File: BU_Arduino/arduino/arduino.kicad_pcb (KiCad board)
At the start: 2 copper layers, 52 parts, among them CON1 ICSP, J1 USB_A, J2 Barrel_Jack, J3 Power, J4 Digital, J5 Digital, J6 Analog, Q1 FDN340P, SW1 SW_Push_Dual, U1 NCP1117-12_TO252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

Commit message: Updated PCB Design Files
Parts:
- CON1, J3, J4, J5, J6: moved to F.Cu
- moved U1 145.3 mm to (102.5, 114.2), turned to 180 degrees
- moved J2 131.0 mm to (107.5, 124.3), turned to 0 degrees
- moved J3 125.3 mm to (144.4, 130.0), turned to 90 degrees
- moved U2 96.1 mm to (153.4, 104.9), turned to 180 degrees
- moved J1 87.6 mm to (182.1, 118.9), turned to 90 degrees
- moved J6 85.0 mm to (180.0, 130.0), turned to 270 degrees
- moved J4 82.1 mm to (135.3, 82.0), turned to 90 degrees
- moved CON1 69.2 mm to (182.6, 102.4), turned to 0 degrees
- moved J5 64.1 mm to (162.2, 82.0), turned to 90 degrees
- moved C15 63.0 mm to (124.6, 123.3)
- moved Q1 61.6 mm to (118.8, 111.6), turned to 180 degrees
- moved U4 58.8 mm to (102.1, 106.3)
- moved C3 49.7 mm to (109.9, 104.9)
- moved C22 47.5 mm to (102.8, 98.7), turned to 180 degrees
- moved C9 46.3 mm to (115.7, 123.3)
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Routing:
- net GND: track 18.2 -> 373.9 mm, vias 0 -> 9
- net +5V: track 19.0 -> 230.7 mm, vias 0 -> 12
- net /D7: track 0.00 -> 98.7 mm, vias 0 -> 3
- net +3V3: track 0.00 -> 97.9 mm, vias 0 -> 1
- net /VUSB: track 0.00 -> 74.4 mm, vias 0 -> 2
- net /D3/SCL: track 0.00 -> 72.5 mm, vias 0 -> 1
- net /VIN: track 16.1 -> 87.7 mm, vias 0 -> 1
- net /IO13: track 0.00 -> 71.0 mm, vias 0 -> 2
- net /D2/SDA: track 0.00 -> 69.0 mm, vias 0 -> 1
- net Net-(C16-Pad1): track 0.00 -> 59.0 mm, vias 0 -> 2
- net /D5: track 0.00 -> 59.0 mm, vias 0 -> 1
- net Net-(CON1-Pad5): track 0.00 -> 51.4 mm
- net /D0/RX: track 0.00 -> 47.8 mm, vias 0 -> 1
- net /AREF: track 0.00 -> 45.6 mm, vias 0 -> 4
- net /D6: track 0.00 -> 45.5 mm
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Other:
- board outline added: 89.7 x 55.1 mm
- board text added: "BUduino"

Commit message: Updated few files
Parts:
- C16, C18, C4, C5, C6, C8: footprint Capacitors_SMD:C_0805_HandSoldering -> Capacitors_SMD:C_0603_HandSoldering
- moved C8 100.8 mm to (204.0, 100.6)
- moved C21 82.7 mm to (183.7, 120.1)
- moved C22 76.9 mm to (179.3, 106.4)
- moved C3 62.8 mm to (170.7, 120.4), turned to 270 degrees
- moved C5 60.4 mm to (166.1, 118.4), turned to 270 degrees
- moved U4 56.4 mm to (158.5, 105.7)
- moved R11 50.9 mm to (161.3, 116.8), turned to 0 degrees
- moved SW1 46.2 mm to (209.8, 95.2), turned to 180 degrees
- moved U1 44.1 mm to (146.6, 115.3)
- moved D6 42.4 mm to (163.6, 104.6), turned to 270 degrees
- moved U3 41.4 mm to (156.5, 111.8), turned to 90 degrees
- moved D2 40.6 mm to (155.7, 121.4)
- moved R12 40.1 mm to (161.8, 108.7)
- moved R6 39.5 mm to (179.8, 117.9), turned to 90 degrees
- moved J2 38.1 mm to (145.5, 126.5)
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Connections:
- C6 pad 1: Net-(C6-Pad1) -> /AREF
- CON1 pad 5: Net-(CON1-Pad5) -> /RST
- D1 pad 2: Net-(CON1-Pad5) -> /RST
- J3 pad 3: /RESET -> /RST
- R3 pad 2: Net-(CON1-Pad5) -> /RST
- SW1 pad 1: Net-(CON1-Pad5) -> /RST
- U2 pad 13: Net-(CON1-Pad5) -> /RST
- U2 pad 42: Net-(C6-Pad1) -> /AREF
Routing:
- net /RST: track 0.00 -> 104.0 mm, vias 0 -> 4
- net Net-(CON1-Pad5): track 51.4 -> 0.00 mm
- net Net-(C16-Pad1): track 59.0 -> 10.6 mm, vias 2 -> 0
- net +3V3: track 97.9 -> 64.1 mm
- net /AREF: track 45.6 -> 73.4 mm, vias 4 -> 3
- net /D7: track 98.7 -> 73.6 mm, vias 3 -> 1
- net GND: track 373.9 -> 349.8 mm, vias 9 -> 11
- net /D2/SDA: track 69.0 -> 91.9 mm
- net /IO11: track 27.3 -> 46.2 mm
- net Net-(J1-Pad1): track 24.0 -> 5.67 mm, vias 2 -> 0
- net /VIN: track 87.7 -> 70.2 mm, vias 1 -> 2
- net /D0/RX: track 47.8 -> 31.1 mm
- net /IO13: track 71.0 -> 54.3 mm
- net Net-(C7-Pad2): track 27.9 -> 14.8 mm, vias 2 -> 0
- net Net-(J1-Pad2): track 18.5 -> 6.22 mm
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- added copper zone on B.Cu, net GND
- added copper zone on F.Cu, net GND
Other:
- board size 89.7 x 55.1 mm -> 78.2 x 55.6 mm

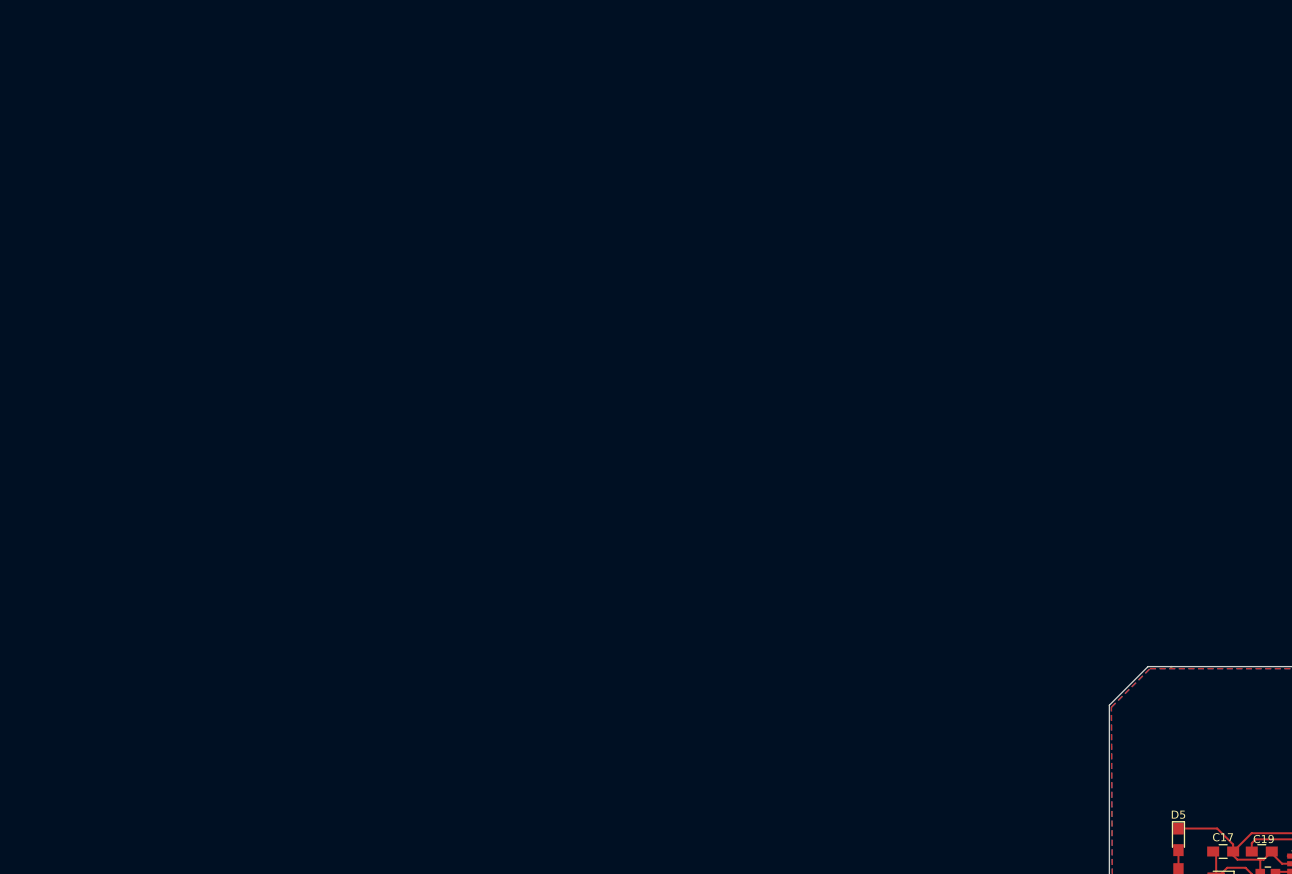
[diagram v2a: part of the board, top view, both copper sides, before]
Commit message: Added gnd planes stiching Vias
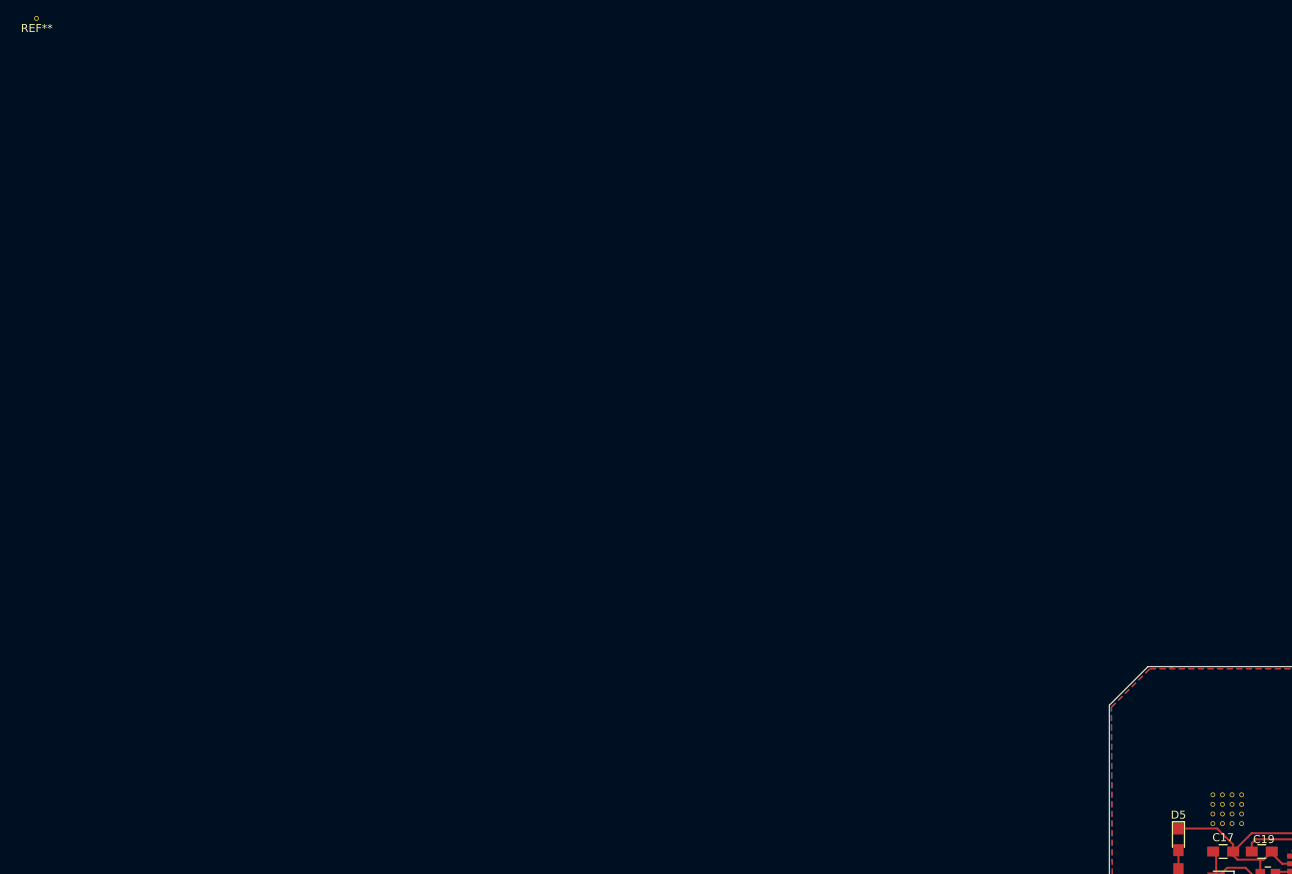
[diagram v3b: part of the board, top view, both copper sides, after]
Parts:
- added REF**: Via, arduino:Via, F.Cu at (150.7, 100.6)
- added REF**: Via, arduino:Via, F.Cu at (149.5, 98.2)
- added REF**: Via, arduino:Via, F.Cu at (148.3, 98.2)
- added REF**: Via, arduino:Via, F.Cu at (147.1, 98.2)
- added REF**: Via, arduino:Via, F.Cu at (150.7, 97.0)
- added REF**: Via, arduino:Via, F.Cu at (149.5, 97.0)
- added REF**: Via, arduino:Via, F.Cu at (148.3, 97.0)
- added REF**: Via-0.6mm, Via-0.6mm, F.Cu at (0.00, 0.00)
- added REF**: Via, arduino:Via, F.Cu at (147.1, 97.0)
- added REF**: Via, arduino:Via, F.Cu at (149.5, 100.6)
- added REF**: Via, arduino:Via, F.Cu at (148.3, 100.6)
- added REF**: Via, arduino:Via, F.Cu at (147.1, 100.6)
- added REF**: Via, arduino:Via, F.Cu at (150.7, 99.4)
- added REF**: Via, arduino:Via, F.Cu at (149.5, 99.4)
- added REF**: Via, arduino:Via, F.Cu at (148.3, 99.4)
- added REF**: Via, arduino:Via, F.Cu at (147.1, 99.4)
- added REF**: Via, arduino:Via, F.Cu at (150.7, 98.2)
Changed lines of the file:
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@@
 (kicad_pcb (version 4) (host pcbnew 4.0.7)
   (general
-    (links 145)
+    (links 161)
     (no_connects 0)
-    (area 131.316999 80.975999 212.511001 136.965)
+    (area -4.571904 -2.105 212.511001 136.965)
     (thickness 1.6)
     (drawings 16)
     (tracks 755)
     (zones 0)
-    (modules 52)
+    (modules 69)
     (nets 52)
   )
@@
     (mod_text_size 1 1)
     (mod_text_width 0.15)
-    (pad_size 1.2 0.75)
-    (pad_drill 0)
+    (pad_size 0.6 0.6)
+    (pad_drill 0.4)
     (pad_to_mask_clearance 0)
     (aux_axis_origin 0 0)
@@
       (psa4output false)
       (plotreference true)
-      (plotvalue true)
+      (plotvalue false)
       (plotinvisibletext false)
       (padsonsilk false)
@@
     (add_net "Net-(U4-Pad4)")
   )
+  (module arduino:Via (layer F.Cu)
+    (at 150.666 100.628)
+    (fp_text reference REF** (at 0.05 1.58) (layer F.SilkS) hide
+      (effects (font (size 1 1) (thickness 0.15)))
+    )
+    (fp_text value Via (at 0.01 -1.78) (layer F.Fab) hide
+      (effects (font (size 1 1) (thickness 0.15)))
+    )
+    (pad 1 thru_hole circle (at -0.02 0.02) (size 0.6 0.6) (drill 0.4) (layers *.Cu)
+      (net 2 GND) (zone_connect 2))
+  )
+  (module arduino:Via (layer F.Cu)
+    (at 149.466 100.628)
+    (fp_text reference REF** (at 0.05 1.58) (layer F.SilkS) hide
+      (effects (font (size 1 1) (thickness 0.15)))
+    )
+    (fp_text value Via (at 0.01 -1.78) (layer F.Fab) hide
+      (effects (font (size 1 1) (thickness 0.15)))
+    )
+    (pad 1 thru_hole circle (at -0.02 0.02) (size 0.6 0.6) (drill 0.4) (layers *.Cu)
+      (net 2 GND) (zone_connect 2))
+  )
+  (module arduino:Via (layer F.Cu)
+    (at 148.266 100.628)
+    (fp_text reference REF** (at 0.05 1.58) (layer F.SilkS) hide
+      (effects (font (size 1 1) (thickness 0.15)))
+    )
+    (fp_text value Via (at 0.01 -1.78) (layer F.Fab) hide
+      (effects (font (size 1 1) (thickness 0.15)))
+    )
+    (pad 1 thru_hole circle (at -0.02 0.02) (size 0.6 0.6) (drill 0.4) (layers *.Cu)
+      (net 2 GND) (zone_connect 2))
+  )
+  (module arduino:Via (layer F.Cu)
+    (at 147.066 100.628)
+    (fp_text reference REF** (at 0.05 1.58) (layer F.SilkS) hide
+      (effects (font (size 1 1) (thickness 0.15)))
+    )
+    (fp_text value Via (at 0.01 -1.78) (layer F.Fab) hide
+      (effects (font (size 1 1) (thickness 0.15)))
+    )
+    (pad 1 thru_hole circle (at -0.02 0.02) (size 0.6 0.6) (drill 0.4) (layers *.Cu)
+      (net 2 GND) (zone_connect 2))
+  )
+  (module arduino:Via (layer F.Cu)
+    (at 150.666 99.428)
+    (fp_text reference REF** (at 0.05 1.58) (layer F.SilkS) hide
+      (effects (font (size 1 1) (thickness 0.15)))
+    )
+    (fp_text value Via (at 0.01 -1.78) (layer F.Fab) hide
+      (effects (font (size 1 1) (thickness 0.15)))
+    )
+    (pad 1 thru_hole circle (at -0.02 0.02) (size 0.6 0.6) (drill 0.4) (layers *.Cu)
+      (net 2 GND) (zone_connect 2))
+  )
+  (module arduino:Via (layer F.Cu)
+    (at 149.466 99.428)
+    (fp_text reference REF** (at 0.05 1.58) (layer F.SilkS) hide
+      (effects (font (size 1 1) (thickness 0.15)))
+    )
+    (fp_text value Via (at 0.01 -1.78) (layer F.Fab) hide
+      (effects (font (size 1 1) (thickness 0.15)))
+    )
+    (pad 1 thru_hole circle (at -0.02 0.02) (size 0.6 0.6) (drill 0.4) (layers *.Cu)
+      (net 2 GND) (zone_connect 2))
+  )
+  (module arduino:Via (layer F.Cu)
+    (at 148.266 99.428)
+    (fp_text reference REF** (at 0.05 1.58) (layer F.SilkS) hide
+      (effects (font (size 1 1) (thickness 0.15)))
+    )
+    (fp_text value Via (at 0.01 -1.78) (layer F.Fab) hide
+      (effects (font (size 1 1) (thickness 0.15)))
+    )
+    (pad 1 thru_hole circle (at -0.02 0.02) (size 0.6 0.6) (drill 0.4) (layers *.Cu)
+      (net 2 GND) (zone_connect 2))
+  )
+  (module arduino:Via (layer F.Cu)
+    (at 147.066 99.428)
+    (fp_text reference REF** (at 0.05 1.58) (layer F.SilkS) hide
+      (effects (font (size 1 1) (thickness 0.15)))
+    )
+    (fp_text value Via (at 0.01 -1.78) (layer F.Fab) hide
+      (effects (font (size 1 1) (thickness 0.15)))
+    )
+    (pad 1 thru_hole circle (at -0.02 0.02) (size 0.6 0.6) (drill 0.4) (layers *.Cu)
+      (net 2 GND) (zone_connect 2))
+  )
+  (module arduino:Via (layer F.Cu)
+    (at 150.666 98.228)
+    (fp_text reference REF** (at 0.05 1.58) (layer F.SilkS) hide
+      (effects (font (size 1 1) (thickness 0.15)))
+    )
+    (fp_text value Via (at 0.01 -1.78) (layer F.Fab) hide
+      (effects (font (size 1 1) (thickness 0.15)))
+    )
+    (pad 1 thru_hole circle (at -0.02 0.02) (size 0.6 0.6) (drill 0.4) (layers *.Cu)
+      (net 2 GND) (zone_connect 2))
+  )
+  (module arduino:Via (layer F.Cu)
+    (at 149.466 98.228)
+    (fp_text reference REF** (at 0.05 1.58) (layer F.SilkS) hide
+      (effects (font (size 1 1) (thickness 0.15)))
+    )
+    (fp_text value Via (at 0.01 -1.78) (layer F.Fab) hide
+      (effects (font (size 1 1) (thickness 0.15)))
+    )
+    (pad 1 thru_hole circle (at -0.02 0.02) (size 0.6 0.6) (drill 0.4) (layers *.Cu)
+      (net 2 GND) (zone_connect 2))
+  )
+  (module arduino:Via (layer F.Cu)
+    (at 148.266 98.228)
+    (fp_text reference REF** (at 0.05 1.58) (layer F.SilkS) hide
+      (effects (font (size 1 1) (thickness 0.15)))
+    )
+    (fp_text value Via (at 0.01 -1.78) (layer F.Fab) hide
+      (effects (font (size 1 1) (thickness 0.15)))
+    )
+    (pad 1 thru_hole circle (at -0.02 0.02) (size 0.6 0.6) (drill 0.4) (layers *.Cu)
+      (net 2 GND) (zone_connect 2))
+  )
+  (module arduino:Via (layer F.Cu)
+    (at 147.066 98.228)
+    (fp_text reference REF** (at 0.05 1.58) (layer F.SilkS) hide
+      (effects (font (size 1 1) (thickness 0.15)))
+    )
+    (fp_text value Via (at 0.01 -1.78) (layer F.Fab) hide
+      (effects (font (size 1 1) (thickness 0.15)))
+    )
+    (pad 1 thru_hole circle (at -0.02 0.02) (size 0.6 0.6) (drill 0.4) (layers *.Cu)
+      (net 2 GND) (zone_connect 2))
+  )
+  (module arduino:Via (layer F.Cu)
+    (at 150.666 97.028)
+    (fp_text reference REF** (at 0.05 1.58) (layer F.SilkS) hide
+      (effects (font (size 1 1) (thickness 0.15)))
+    )
+    (fp_text value Via (at 0.01 -1.78) (layer F.Fab) hide
+      (effects (font (size 1 1) (thickness 0.15)))
+    )
+    (pad 1 thru_hole circle (at -0.02 0.02) (size 0.6 0.6) (drill 0.4) (layers *.Cu)
+      (net 2 GND) (zone_connect 2))
+  )
+  (module arduino:Via (layer F.Cu)
+    (at 149.466 97.028)
+    (fp_text reference REF** (at 0.05 1.58) (layer F.SilkS) hide
+      (effects (font (size 1 1) (thickness 0.15)))
+    )
+    (fp_text value Via (at 0.01 -1.78) (layer F.Fab) hide
+      (effects (font (size 1 1) (thickness 0.15)))
+    )
+    (pad 1 thru_hole circle (at -0.02 0.02) (size 0.6 0.6) (drill 0.4) (layers *.Cu)
+      (net 2 GND) (zone_connect 2))
+  )
+  (module arduino:Via (layer F.Cu)
+    (at 148.266 97.028)
+    (fp_text reference REF** (at 0.05 1.58) (layer F.SilkS) hide
+      (effects (font (size 1 1) (thickness 0.15)))
+    )
+    (fp_text value Via (at 0.01 -1.78) (layer F.Fab) hide
+      (effects (font (size 1 1) (thickness 0.15)))
+    )
+    (pad 1 thru_hole circle (at -0.02 0.02) (size 0.6 0.6) (drill 0.4) (layers *.Cu)
+      (net 2 GND) (zone_connect 2))
+  )
+  (module Via-0.6mm (layer F.Cu)
+    (at 0 0)
+    (fp_text reference REF** (at 0.04 1.24) (layer F.SilkS)
+      (effects (font (size 1 1) (thickness 0.15)))
+    )
+    (fp_text value Via-0.6mm (at -0.11 -1.13) (layer F.Fab)
+      (effects (font (size 1 1) (thickness 0.15)))
+    )
+    (pad 1 thru_hole circle (at 0 0) (size 0.6 0.6) (drill 0.4) (layers *.Cu)
+      (zone_connect 2))
+  )
   (module Capacitors_SMD:C_0805_HandSoldering (layer F.Cu)
     (at 185.42 97.028)
@@
     )
   )
+  (module arduino:Via (layer F.Cu)
+    (at 147.066 97.028)
+    (fp_text reference REF** (at 0.05 1.58) (layer F.SilkS) hide
+      (effects (font (size 1 1) (thickness 0.15)))
+    )
+    (fp_text value Via (at 0.01 -1.78) (layer F.Fab) hide
+      (effects (font (size 1 1) (thickness 0.15)))
+    )
+    (pad 1 thru_hole circle (at -0.02 0.02) (size 0.6 0.6) (drill 0.4) (layers *.Cu)
+      (net 2 GND) (zone_connect 2))
+  )
   (gr_line (start 210.566 81.026) (end 208.026 81.026) (angle 90) (layer Edge.Cuts) (width 0.1))
